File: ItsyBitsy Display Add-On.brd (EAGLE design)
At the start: 35.6 x 17.8 mm, 18 parts, among them IC1 APX803, SW1 SPST_TACT-KMR2

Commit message: Small silkscreen changes
nothing to hardware changed
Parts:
- removed $$U$1: (no value), silks:ITSYM4_TOP
- removed $$U$2: (no value), microbuilder:ADAFRUIT_5MM
- removed U$100: (no value), silks:ITSYM4_BOT
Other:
- board text removed: "i2c address 0x3C"
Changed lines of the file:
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@@
 <?xml version="1.0" encoding="utf-8"?>
 <!DOCTYPE eagle SYSTEM "eagle.dtd">
-<eagle version="9.5.1">
+<eagle version="9.6.2">
 <drawing>
 <settings>
-<setting alwaysvectorfont="no"/>
+<setting alwaysvectorfont="yes"/>
 <setting keepoldvectorfont="yes"/>
 <setting verticaltext="up"/>
@@
 <grid distance="5" unitdist="mil" unit="inch" style="lines" multiple="1" display="no" altdistance="1" altunitdist="mil" altunit="mil"/>
 <layers>
-<layer number="1" name="Top" color="4" fill="1" visible="no" active="yes"/>
+<layer number="1" name="Top" color="4" fill="1" visible="yes" active="yes"/>
 <layer number="2" name="Route2" color="1" fill="3" visible="no" active="yes"/>
 <layer number="3" name="Route3" color="4" fill="3" visible="no" active="no"/>
@@
 <layer number="19" name="Unrouted" color="6" fill="1" visible="yes" active="yes"/>
 <layer number="20" name="Dimension" color="15" fill="1" visible="yes" active="yes"/>
-<layer number="21" name="tPlace" color="14" fill="1" visible="no" active="yes"/>
+<layer number="21" name="tPlace" color="14" fill="1" visible="yes" active="yes"/>
 <layer number="22" name="bPlace" color="13" fill="1" visible="yes" active="yes"/>
-<layer number="23" name="tOrigins" color="14" fill="1" visible="no" active="yes"/>
+<layer number="23" name="tOrigins" color="14" fill="1" visible="yes" active="yes"/>
 <layer number="24" name="bOrigins" color="13" fill="1" visible="yes" active="yes"/>
-<layer number="25" name="tNames" color="7" fill="1" visible="no" active="yes"/>
+<layer number="25" name="tNames" color="7" fill="1" visible="yes" active="yes"/>
 <layer number="26" name="bNames" color="7" fill="1" visible="yes" active="yes"/>
-<layer number="27" name="tValues" color="7" fill="1" visible="no" active="yes"/>
-<layer number="28" name="bValues" color="7" fill="1" visible="no" active="yes"/>
-<layer number="29" name="tStop" color="7" fill="3" visible="no" active="yes"/>
-<layer number="30" name="bStop" color="7" fill="6" visible="no" active="yes"/>
-<layer number="31" name="tCream" color="7" fill="4" visible="no" active="yes"/>
-<layer number="32" name="bCream" color="7" fill="5" visible="no" active="yes"/>
+<layer number="27" name="tValues" color="7" fill="1" visible="yes" active="yes"/>
+<layer number="28" name="bValues" color="7" fill="1" visible="yes" active="yes"/>
+<layer number="29" name="tStop" color="7" fill="3" visible="yes" active="yes"/>
+<layer number="30" name="bStop" color="7" fill="6" visible="yes" active="yes"/>
+<layer number="31" name="tCream" color="7" fill="4" visible="yes" active="yes"/>
+<layer number="32" name="bCream" color="7" fill="5" visible="yes" active="yes"/>
 <layer number="33" name="tFinish" color="6" fill="3" visible="no" active="yes"/>
 <layer number="34" name="bFinish" color="6" fill="6" visible="no" active="yes"/>
 <layer number="35" name="tGlue" color="7" fill="4" visible="no" active="yes"/>
-<layer number="36" name="bGlue" color="7" fill="5" visible="no" active="yes"/>
+<layer number="36" name="bGlue" color="7" fill="5" visible="yes" active="yes"/>
 <layer number="37" name="tTest" color="7" fill="1" visible="no" active="yes"/>
 <layer number="38" name="bTest" color="7" fill="1" visible="no" active="yes"/>
@@
 <layer number="42" name="bRestrict" color="1" fill="10" visible="yes" active="yes"/>
 <layer number="43" name="vRestrict" color="2" fill="10" visible="no" active="yes"/>
-<layer number="44" name="Drills" color="7" fill="1" visible="no" active="yes"/>
+<layer number="44" name="Drills" color="7" fill="1" visible="yes" active="yes"/>
 <layer number="45" name="Holes" color="7" fill="1" visible="no" active="yes"/>
 <layer number="46" name="Milling" color="3" fill="1" visible="no" active="yes"/>
@@
 <layer number="49" name="Reference" color="7" fill="1" visible="no" active="yes"/>
 <layer number="50" name="dxf" color="7" fill="1" visible="no" active="no"/>
-<layer number="51" name="tDocu" color="7" fill="1" visible="no" active="yes"/>
+<layer number="51" name="tDocu" color="7" fill="1" visible="yes" active="yes"/>
 <layer number="52" name="bDocu" color="7" fill="1" visible="yes" active="yes"/>
 <layer number="53" name="tGND_GNDA" color="7" fill="9" visible="no" active="no"/>
@@
 <wire x1="3.175" y1="15.367" x2="3.175" y2="5.334" width="0" layer="20"/>
 <wire x1="3.175" y1="5.334" x2="0" y2="5.334" width="0" layer="20"/>
-<text x="24.765" y="6.731" size="1.016" layer="22" font="vector" ratio="12" rot="MR0" align="center">i2c address 0x3C</text>
-<text x="25.019" y="9.398" size="1.27" layer="22" font="vector" ratio="12" rot="MR0" align="center">128x32 Monochrome
+<text x="25.908" y="9.017" size="1.016" layer="22" font="vector" ratio="12" distance="30" rot="MR0" align="center">128x32 Monochrome
 OLED BitsyWing</text>
-<text x="6.35" y="14.986" size="1.016" layer="22" font="vector" ratio="12" rot="MR0" align="center">HEXTHAT</text>
+<text x="25.908" y="5.334" size="1.4224" layer="22" font="vector" ratio="14" rot="MR0" align="center">HEXTHAT</text>
 </plain>
 <attributes>
@@
 <attribute name="VALUE" x="35.56" y="4.445" size="0.4064" layer="27" ratio="10" rot="R180"/>
 </element>
-<element name="$$U$1" library="silks" package="ITSYM4_TOP" value="" x="0" y="0" smashed="yes"/>
-<element name="U$100" library="silks" package="ITSYM4_BOT" value="" x="35.56" y="0" smashed="yes" rot="MR0"/>
 <element name="OLED" library="microbuilder" package="UG-2832HSWEG02_WRAPUNDER" value="OLED 128x32" x="5.461" y="9.017" smashed="yes" rot="R180">
 <attribute name="NAME" x="23.65" y="6.581" size="0.8128" layer="25" ratio="18" rot="R180"/>
@@
 <attribute name="VALUE" x="5.588" y="5.08" size="0.4064" layer="28" ratio="10" rot="MR180"/>
 </element>
-<element name="$$U$2" library="microbuilder" package="ADAFRUIT_5MM" value="" x="22.987" y="11.049" smashed="yes" rot="MR0"/>
 </elements>
 <signals>
@@
 </signals>
 <mfgpreviewcolors>
-<mfgpreviewcolor name="soldermaskcolor" color="0xC8008000"/>
+<mfgpreviewcolor name="soldermaskcolor" color="0xC8000000"/>
 <mfgpreviewcolor name="silkscreencolor" color="0xFFFEFEFE"/>
-<mfgpreviewcolor name="backgroundcolor" color="0xFF282828"/>
+<mfgpreviewcolor name="backgroundcolor" color="0xFFFFFFFF"/>
 <mfgpreviewcolor name="coppercolor" color="0xFFFFBF00"/>
 <mfgpreviewcolor name="substratecolor" color="0xFF786E46"/>

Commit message: Fixed No ground to OLED, added names
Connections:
- net N$1 renamed C2P
- net N$2 renamed C2N
- net N$3 renamed C1P
- net N$4 renamed C1N
- net N$5 renamed VCOMH
- net N$6 renamed VCC
- net N$7 renamed IREF
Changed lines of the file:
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@@
 <layers>
 <layer number="1" name="Top" color="4" fill="1" visible="yes" active="yes"/>
-<layer number="2" name="Route2" color="1" fill="3" visible="no" active="yes"/>
+<layer number="2" name="Route2" color="1" fill="3" visible="yes" active="yes"/>
 <layer number="3" name="Route3" color="4" fill="3" visible="no" active="no"/>
 <layer number="4" name="Route4" color="1" fill="4" visible="no" active="no"/>
@@
 <layer number="13" name="Route13" color="4" fill="5" visible="no" active="no"/>
 <layer number="14" name="Route14" color="1" fill="6" visible="no" active="no"/>
-<layer number="15" name="Route15" color="4" fill="6" visible="no" active="yes"/>
+<layer number="15" name="Route15" color="4" fill="6" visible="yes" active="yes"/>
 <layer number="16" name="Bottom" color="9" fill="1" visible="yes" active="yes"/>
 <layer number="17" name="Pads" color="2" fill="1" visible="yes" active="yes"/>
@@
 <contactref element="OLED" pad="6"/>
 </signal>
-<signal name="N$1">
+<signal name="C2P">
 <contactref element="OLED" pad="1"/>
 <contactref element="C5" pad="2"/>
@@
 <wire x1="12.478" y1="14.317" x2="12.7" y2="14.539" width="0.2032" layer="16"/>
 </signal>
-<signal name="N$2">
+<signal name="C2N">
 <contactref element="C5" pad="1"/>
 <contactref element="OLED" pad="2"/>
@@
 <wire x1="11.642" y1="13.697" x2="7.491" y2="13.697" width="0.2032" layer="16"/>
 </signal>
-<signal name="N$3">
+<signal name="C1P">
 <contactref element="OLED" pad="3"/>
 <contactref element="C4" pad="2"/>
@@
 <wire x1="13.8818" y1="14.224" x2="13.8818" y2="12.01975" width="0.2032" layer="16"/>
 </signal>
-<signal name="N$4">
+<signal name="C1N">
 <contactref element="C4" pad="1"/>
 <contactref element="OLED" pad="4"/>
@@
 <wire x1="10.276" y1="12.457" x2="7.491" y2="12.457" width="0.2032" layer="16"/>
 </signal>
-<signal name="N$5">
+<signal name="VCOMH">
 <contactref element="OLED" pad="13"/>
 <contactref element="C2" pad="2"/>
@@
 <wire x1="13.382" y1="6.877" x2="13.655" y2="6.604" width="0.2032" layer="16"/>
 </signal>
-<signal name="N$7">
+<signal name="IREF">
 <contactref element="OLED" pad="12"/>
 <contactref element="R1" pad="2"/>
@@
 <wire x1="12.323" y1="7.497" x2="13.208" y2="8.382" width="0.2032" layer="16"/>
 </signal>
-<signal name="N$6">
+<signal name="VCC">
 <contactref element="OLED" pad="14"/>
 <contactref element="C3" pad="2"/>

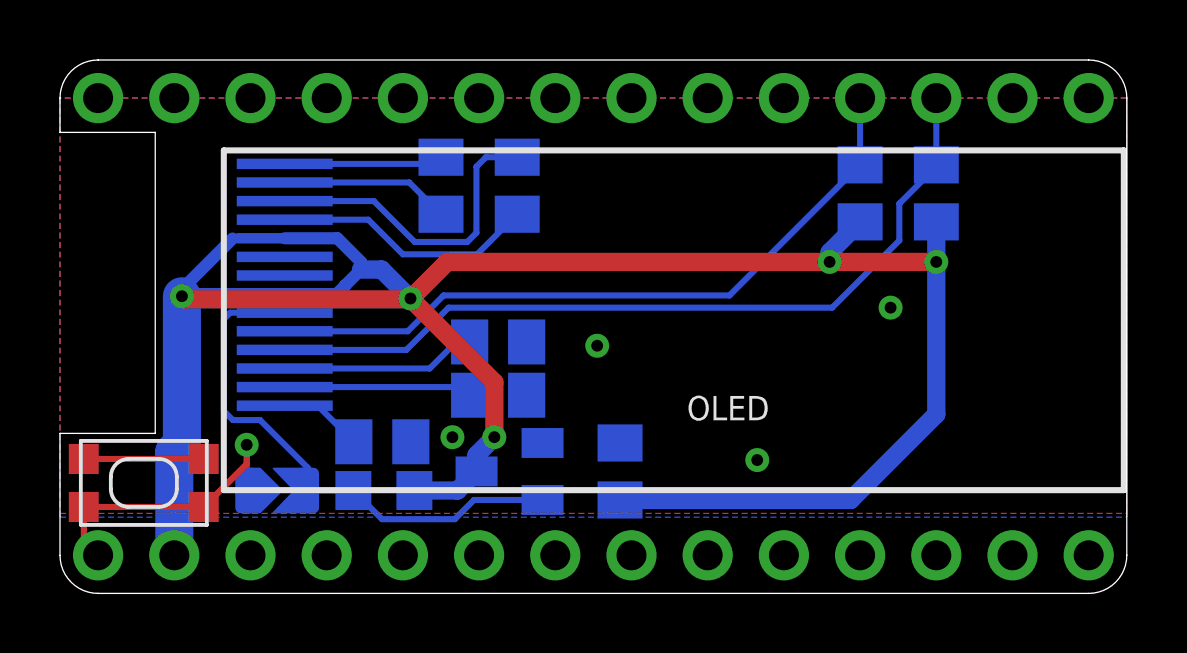
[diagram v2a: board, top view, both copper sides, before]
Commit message: add info about what pad does
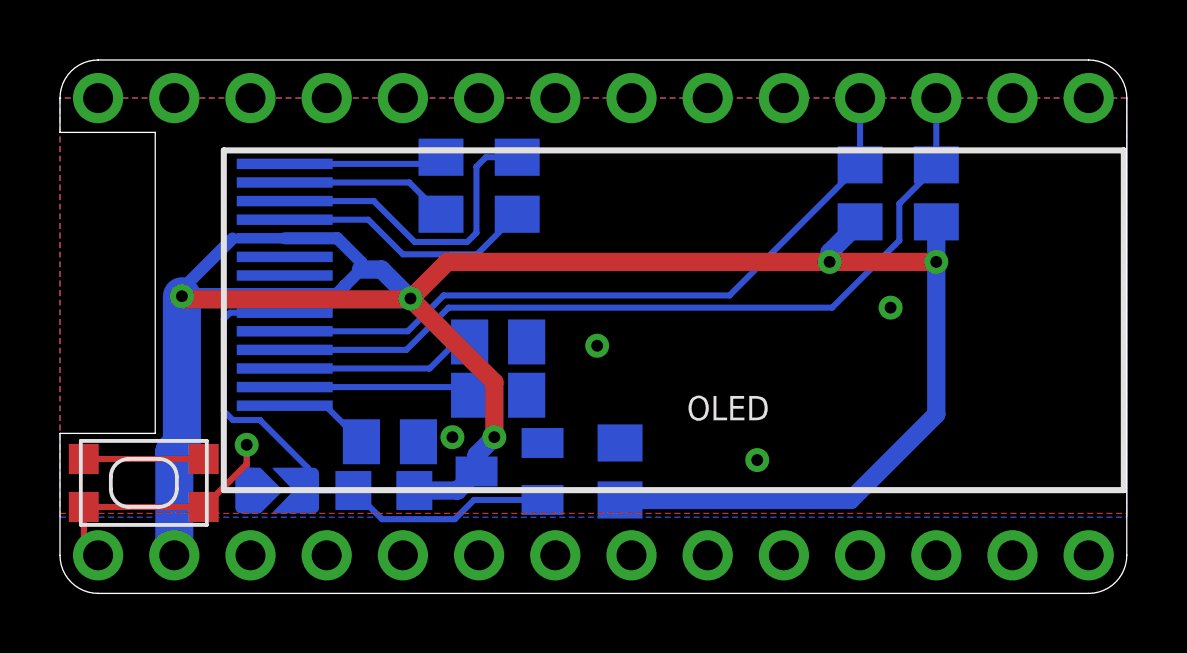
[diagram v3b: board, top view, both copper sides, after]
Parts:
- moved C3 0.25 mm to (11.0, 5.05)
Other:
- board text added: "PAD +Board RST to switch"
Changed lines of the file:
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@@
 <grid distance="5" unitdist="mil" unit="inch" style="lines" multiple="1" display="no" altdistance="1" altunitdist="mil" altunit="mil"/>
 <layers>
-<layer number="1" name="Top" color="4" fill="1" visible="yes" active="yes"/>
-<layer number="2" name="Route2" color="1" fill="3" visible="yes" active="yes"/>
+<layer number="1" name="Top" color="4" fill="1" visible="no" active="yes"/>
+<layer number="2" name="Route2" color="1" fill="3" visible="no" active="yes"/>
 <layer number="3" name="Route3" color="4" fill="3" visible="no" active="no"/>
 <layer number="4" name="Route4" color="1" fill="4" visible="no" active="no"/>
@@
 <layer number="13" name="Route13" color="4" fill="5" visible="no" active="no"/>
 <layer number="14" name="Route14" color="1" fill="6" visible="no" active="no"/>
-<layer number="15" name="Route15" color="4" fill="6" visible="yes" active="yes"/>
+<layer number="15" name="Route15" color="4" fill="6" visible="no" active="yes"/>
 <layer number="16" name="Bottom" color="9" fill="1" visible="yes" active="yes"/>
 <layer number="17" name="Pads" color="2" fill="1" visible="yes" active="yes"/>
@@
 <layer number="19" name="Unrouted" color="6" fill="1" visible="yes" active="yes"/>
 <layer number="20" name="Dimension" color="15" fill="1" visible="yes" active="yes"/>
-<layer number="21" name="tPlace" color="14" fill="1" visible="yes" active="yes"/>
+<layer number="21" name="tPlace" color="14" fill="1" visible="no" active="yes"/>
 <layer number="22" name="bPlace" color="13" fill="1" visible="yes" active="yes"/>
-<layer number="23" name="tOrigins" color="14" fill="1" visible="yes" active="yes"/>
+<layer number="23" name="tOrigins" color="14" fill="1" visible="no" active="yes"/>
 <layer number="24" name="bOrigins" color="13" fill="1" visible="yes" active="yes"/>
-<layer number="25" name="tNames" color="7" fill="1" visible="yes" active="yes"/>
+<layer number="25" name="tNames" color="7" fill="1" visible="no" active="yes"/>
 <layer number="26" name="bNames" color="7" fill="1" visible="yes" active="yes"/>
-<layer number="27" name="tValues" color="7" fill="1" visible="yes" active="yes"/>
-<layer number="28" name="bValues" color="7" fill="1" visible="yes" active="yes"/>
-<layer number="29" name="tStop" color="7" fill="3" visible="yes" active="yes"/>
-<layer number="30" name="bStop" color="7" fill="6" visible="yes" active="yes"/>
-<layer number="31" name="tCream" color="7" fill="4" visible="yes" active="yes"/>
-<layer number="32" name="bCream" color="7" fill="5" visible="yes" active="yes"/>
+<layer number="27" name="tValues" color="7" fill="1" visible="no" active="yes"/>
+<layer number="28" name="bValues" color="7" fill="1" visible="no" active="yes"/>
+<layer number="29" name="tStop" color="7" fill="3" visible="no" active="yes"/>
+<layer number="30" name="bStop" color="7" fill="6" visible="no" active="yes"/>
+<layer number="31" name="tCream" color="7" fill="4" visible="no" active="yes"/>
+<layer number="32" name="bCream" color="7" fill="5" visible="no" active="yes"/>
 <layer number="33" name="tFinish" color="6" fill="3" visible="no" active="yes"/>
 <layer number="34" name="bFinish" color="6" fill="6" visible="no" active="yes"/>
 <layer number="35" name="tGlue" color="7" fill="4" visible="no" active="yes"/>
-<layer number="36" name="bGlue" color="7" fill="5" visible="yes" active="yes"/>
+<layer number="36" name="bGlue" color="7" fill="5" visible="no" active="yes"/>
 <layer number="37" name="tTest" color="7" fill="1" visible="no" active="yes"/>
 <layer number="38" name="bTest" color="7" fill="1" visible="no" active="yes"/>
@@
 <layer number="42" name="bRestrict" color="1" fill="10" visible="yes" active="yes"/>
 <layer number="43" name="vRestrict" color="2" fill="10" visible="no" active="yes"/>
-<layer number="44" name="Drills" color="7" fill="1" visible="yes" active="yes"/>
+<layer number="44" name="Drills" color="7" fill="1" visible="no" active="yes"/>
 <layer number="45" name="Holes" color="7" fill="1" visible="no" active="yes"/>
 <layer number="46" name="Milling" color="3" fill="1" visible="no" active="yes"/>
@@
 <layer number="49" name="Reference" color="7" fill="1" visible="no" active="yes"/>
 <layer number="50" name="dxf" color="7" fill="1" visible="no" active="no"/>
-<layer number="51" name="tDocu" color="7" fill="1" visible="yes" active="yes"/>
+<layer number="51" name="tDocu" color="7" fill="1" visible="no" active="yes"/>
 <layer number="52" name="bDocu" color="7" fill="1" visible="yes" active="yes"/>
 <layer number="53" name="tGND_GNDA" color="7" fill="9" visible="no" active="no"/>
@@
 OLED BitsyWing</text>
 <text x="25.908" y="5.334" size="1.4224" layer="22" font="vector" ratio="14" rot="MR0" align="center">HEXTHAT</text>
+<text x="15.113" y="10.795" size="0.6096" layer="22" font="vector" ratio="13" distance="20" rot="MR0" align="center">PAD +Board RST
+to switch</text>
 </plain>
 <attributes>
@@
 <attribute name="VALUE" x="19.431" y="2.032" size="0.4064" layer="28" ratio="10" rot="MR270"/>
 </element>
-<element name="C3" library="microbuilder" package="0805-NO" value="10uF" x="10.7442" y="5.0546" smashed="yes" rot="MR0">
-<attribute name="NAME" x="11.3792" y="5.8166" size="0.8128" layer="26" ratio="18" rot="MR0"/>
-<attribute name="VALUE" x="8.7122" y="4.2926" size="0.4064" layer="28" ratio="10" rot="MR0"/>
+<element name="C3" library="microbuilder" package="0805-NO" value="10uF" x="10.9982" y="5.0546" smashed="yes" rot="MR0">
+<attribute name="NAME" x="11.6332" y="5.8166" size="0.8128" layer="26" ratio="18" rot="MR0"/>
+<attribute name="VALUE" x="8.9662" y="4.2926" size="0.4064" layer="28" ratio="10" rot="MR0"/>
 </element>
 <element name="C2" library="microbuilder" package="0805-NO" value="10uF" x="14.605" y="6.604" smashed="yes" rot="MR0">
@@
 <contactref element="OLED" pad="14"/>
 <contactref element="C3" pad="2"/>
-<wire x1="7.491" y1="6.257" x2="8.5918" y2="6.257" width="0.2032" layer="16"/>
-<wire x1="8.5918" y1="6.257" x2="9.7942" y2="5.0546" width="0.2032" layer="16"/>
+<wire x1="7.491" y1="6.257" x2="8.8458" y2="6.257" width="0.2032" layer="16"/>
+<wire x1="8.8458" y1="6.257" x2="10.0482" y2="5.0546" width="0.2032" layer="16"/>
 </signal>
 <signal name="3.3V">

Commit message: Add files via upload
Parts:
- moved C3 0.25 mm to (10.7, 5.05)
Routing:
- net 3.3V: track 77.5 -> 75.1 mm
- net VCC: track 3.06 -> 4.28 mm
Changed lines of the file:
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@@
 <drawing>
 <settings>
-<setting alwaysvectorfont="yes"/>
+<setting alwaysvectorfont="no"/>
 <setting keepoldvectorfont="yes"/>
 <setting verticaltext="up"/>
@@
 OLED BitsyWing</text>
 <text x="25.908" y="5.334" size="1.4224" layer="22" font="vector" ratio="14" rot="MR0" align="center">HEXTHAT</text>
-<text x="15.113" y="10.795" size="0.6096" layer="22" font="vector" ratio="13" distance="20" rot="MR0" align="center">PAD +Board RST
+<text x="16.383" y="11.049" size="0.8128" layer="22" font="vector" ratio="13" distance="20" rot="MR0" align="center">PAD +Board RST
 to switch</text>
 </plain>
@@
 <attribute name="VALUE" x="19.431" y="2.032" size="0.4064" layer="28" ratio="10" rot="MR270"/>
 </element>
-<element name="C3" library="microbuilder" package="0805-NO" value="10uF" x="10.9982" y="5.0546" smashed="yes" rot="MR0">
-<attribute name="NAME" x="11.6332" y="5.8166" size="0.8128" layer="26" ratio="18" rot="MR0"/>
-<attribute name="VALUE" x="8.9662" y="4.2926" size="0.4064" layer="28" ratio="10" rot="MR0"/>
+<element name="C3" library="microbuilder" package="0805-NO" value="10uF" x="10.7442" y="5.0546" smashed="yes" rot="MR0">
+<attribute name="NAME" x="11.3792" y="5.8166" size="0.8128" layer="26" ratio="18" rot="MR0"/>
+<attribute name="VALUE" x="8.7122" y="4.2926" size="0.4064" layer="28" ratio="10" rot="MR0"/>
 </element>
 <element name="C2" library="microbuilder" package="0805-NO" value="10uF" x="14.605" y="6.604" smashed="yes" rot="MR0">
@@
 <contactref element="OLED" pad="14"/>
 <contactref element="C3" pad="2"/>
-<wire x1="7.491" y1="6.257" x2="8.8458" y2="6.257" width="0.2032" layer="16"/>
-<wire x1="8.8458" y1="6.257" x2="10.0482" y2="5.0546" width="0.2032" layer="16"/>
+<wire x1="7.491" y1="6.257" x2="8.5918" y2="6.257" width="0.2032" layer="16"/>
+<wire x1="9.7942" y1="5.0546" x2="9.7942" y2="5.6998" width="0.2032" layer="16"/>
+<wire x1="9.237" y1="6.257" x2="7.491" y2="6.257" width="0.2032" layer="16"/>
+<wire x1="9.7942" y1="5.6998" x2="9.237" y2="6.257" width="0.2032" layer="16"/>
 </signal>
 <signal name="3.3V">
@@
 <contactref element="JP2" pad="13"/>
 <wire x1="3.81" y1="1.27" x2="3.81" y2="4.7117625" width="1.27" layer="16"/>
-<wire x1="4.064" y1="10.1397375" x2="5.753053125" y2="11.828790625" width="0.4064" layer="16"/>
 <wire x1="4.064" y1="9.906" x2="4.064" y2="10.1397375" width="0.4064" layer="16"/>
 </signal>
